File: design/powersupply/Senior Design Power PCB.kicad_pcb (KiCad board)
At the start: 2 copper layers, 70.1 x 32 mm, 16 parts, among them U1 VSSOP-10_3x3mm_P0.5mm, U2 TO-263-5_TabPin3

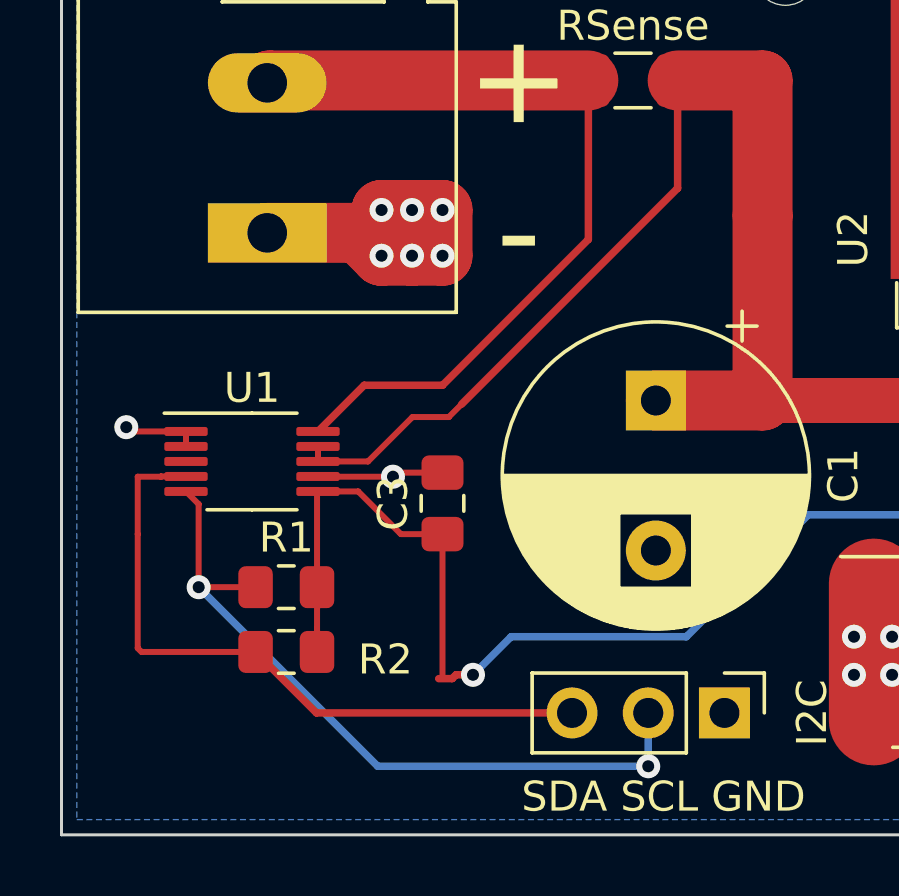
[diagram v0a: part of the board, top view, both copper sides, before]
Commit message: added power supply section
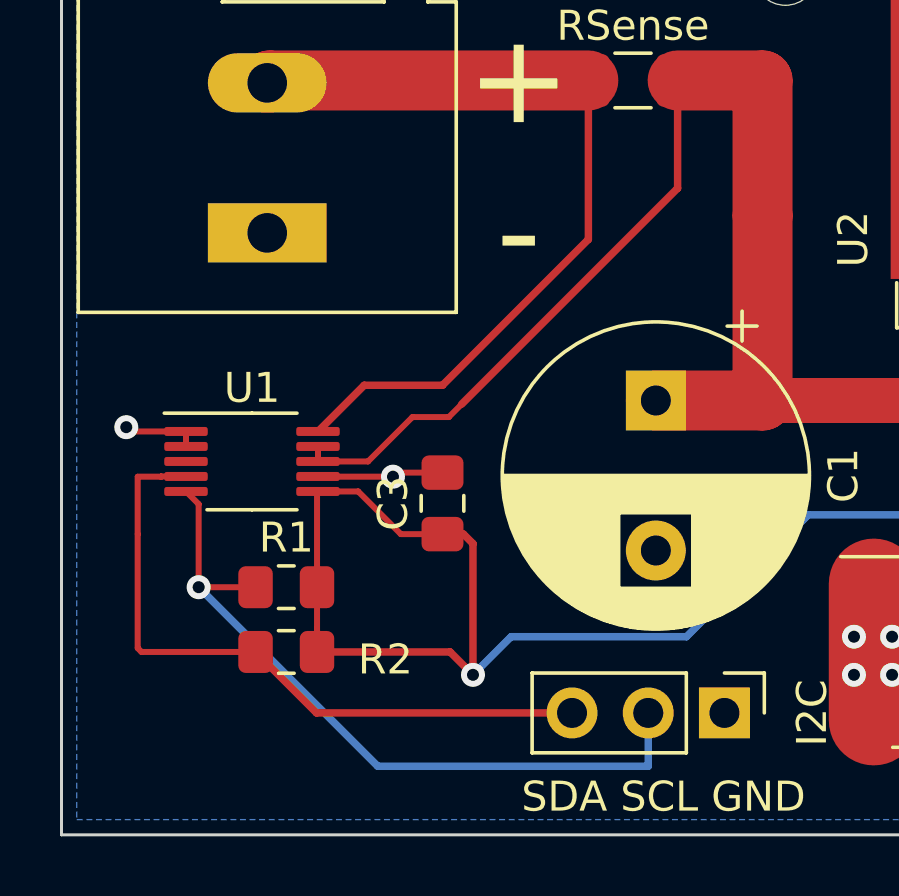
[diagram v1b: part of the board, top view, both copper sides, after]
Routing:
- net B-: track 55.5 -> 40.7 mm, vias 54 -> 48
- net 5V: track 103.9 -> 108.8 mm
- net SCL: vias 2 -> 1
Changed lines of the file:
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@@
-(kicad_pcb (version 20171130) (host pcbnew "(5.1.4)-1")
+(kicad_pcb (version 20171130) (host pcbnew "(5.1.5)-3")
   (general
     (thickness 1.6)
     (drawings 15)
-    (tracks 155)
+    (tracks 138)
     (zones 0)
     (modules 16)
@@
   (segment (start 23.2 36.846) (end 21.352 36.846) (width 0.2) (layer F.Cu) (net 1))
   (segment (start 55.47 30.505) (end 52.07 27.105) (width 1) (layer F.Cu) (net 1))
-  (via (at 29.718 29.464) (size 0.8) (drill 0.4) (layers F.Cu B.Cu) (net 1))
-  (via (at 30.734 29.464) (size 0.8) (drill 0.4) (layers F.Cu B.Cu) (net 1))
-  (via (at 31.75 29.464) (size 0.8) (drill 0.4) (layers F.Cu B.Cu) (net 1))
-  (via (at 31.75 30.988) (size 0.8) (drill 0.4) (layers F.Cu B.Cu) (net 1))
-  (via (at 30.734 30.988) (size 0.8) (drill 0.4) (layers F.Cu B.Cu) (net 1))
-  (via (at 29.718 30.988) (size 0.8) (drill 0.4) (layers F.Cu B.Cu) (net 1))
-  (segment (start 28.956 30.226) (end 29.718 30.988) (width 2) (layer F.Cu) (net 1))
-  (segment (start 29.718 30.988) (end 30.734 30.988) (width 2) (layer F.Cu) (net 1))
-  (segment (start 30.734 30.988) (end 31.75 30.988) (width 2) (layer F.Cu) (net 1))
-  (segment (start 31.75 30.988) (end 31.75 29.464) (width 2) (layer F.Cu) (net 1))
-  (segment (start 30.734 29.464) (end 31.75 29.464) (width 2) (layer F.Cu) (net 1))
-  (segment (start 30.734 29.464) (end 30.734 30.988) (width 2) (layer F.Cu) (net 1))
-  (segment (start 30.734 29.464) (end 29.718 29.464) (width 2) (layer F.Cu) (net 1))
-  (segment (start 29.718 30.988) (end 29.718 29.464) (width 2) (layer F.Cu) (net 1))
   (via (at 45.466 43.688) (size 0.8) (drill 0.4) (layers F.Cu B.Cu) (net 1))
   (via (at 46.736 43.688) (size 0.8) (drill 0.4) (layers F.Cu B.Cu) (net 1))
@@
   (segment (start 55.489 30.463) (end 52.089 27.063) (width 1) (layer F.Cu) (net 1))
   (segment (start 55.489 36.213) (end 55.489 30.463) (width 1) (layer F.Cu) (net 1))
-  (segment (start 29.972 30.226) (end 30.734 29.464) (width 2) (layer F.Cu) (net 1))
-  (segment (start 25.908 30.226) (end 29.972 30.226) (width 2) (layer F.Cu) (net 1))
   (segment (start 22.375 38.346) (end 22.367 38.354) (width 0.2) (layer F.Cu) (net 2))
   (segment (start 23.2 38.346) (end 22.375 38.346) (width 0.2) (layer F.Cu) (net 2))
@@
   (segment (start 27.55 46.228) (end 25.518 44.196) (width 0.25) (layer F.Cu) (net 2))
   (segment (start 36.068 46.228) (end 27.55 46.228) (width 0.25) (layer F.Cu) (net 2))
-  (via (at 38.608 48.006) (size 0.8) (drill 0.4) (layers F.Cu B.Cu) (net 3))
   (via (at 23.622 42.037) (size 0.8) (drill 0.4) (layers F.Cu B.Cu) (net 3))
   (segment (start 25.518 42.037) (end 23.622 42.037) (width 0.2) (layer F.Cu) (net 3))
@@
   (segment (start 27.568 44.285) (end 27.568 42.037) (width 0.2) (layer F.Cu) (net 4))
   (segment (start 27.568 44.196) (end 27.568 43.396) (width 0.2) (layer F.Cu) (net 4))
-  (segment (start 31.75 40.268) (end 31.75 45.085) (width 0.2) (layer F.Cu) (net 4))
   (segment (start 27.568 42.037) (end 27.568 38.998) (width 0.2) (layer F.Cu) (net 4))
-  (segment (start 31.623 45.085) (end 31.75 45.085) (width 0.2) (layer F.Cu) (net 4))
   (segment (start 73.867 40.974) (end 82.296 40.974) (width 3) (layer F.Cu) (net 4))
   (segment (start 70.358 37.465) (end 73.867 40.974) (width 3) (layer F.Cu) (net 4))
@@
   (segment (start 70.358 32.512) (end 70.358 29.96863) (width 3) (layer F.Cu) (net 4))
   (via (at 70.358 32.512) (size 0.8) (drill 0.4) (layers F.Cu B.Cu) (net 4))
-  (segment (start 32.073315 45.085) (end 31.623 45.085) (width 0.25) (layer F.Cu) (net 4))
-  (segment (start 32.200315 44.958) (end 32.073315 45.085) (width 0.25) (layer F.Cu) (net 4))
-  (segment (start 32.766 44.958) (end 32.200315 44.958) (width 0.25) (layer F.Cu) (net 4))
   (segment (start 63.246 39.624) (end 70.358 32.512) (width 0.25) (layer B.Cu) (net 4))
   (segment (start 53.848 39.624) (end 63.246 39.624) (width 0.25) (layer B.Cu) (net 4))
@@
   (segment (start 43.942 39.624) (end 39.878 43.688) (width 0.25) (layer B.Cu) (net 4))
   (segment (start 64.77 26.69) (end 64.77 27.94) (width 0.25) (layer F.Cu) (net 4))
+  (segment (start 32.45 40.268) (end 31.75 40.268) (width 0.25) (layer F.Cu) (net 4))
+  (segment (start 32.766 40.584) (end 32.45 40.268) (width 0.25) (layer F.Cu) (net 4))
+  (segment (start 32.766 44.958) (end 32.766 40.584) (width 0.25) (layer F.Cu) (net 4))
+  (segment (start 32.004 44.196) (end 32.766 44.958) (width 0.25) (layer F.Cu) (net 4))
+  (segment (start 27.568 44.196) (end 32.004 44.196) (width 0.25) (layer F.Cu) (net 4))
   (segment (start 27.6 37.846) (end 27.6 37.346) (width 0.2) (layer F.Cu) (net 5))
   (segment (start 39.5875 25.146) (end 39.5875 28.7385) (width 0.25) (layer F.Cu) (net 5))
